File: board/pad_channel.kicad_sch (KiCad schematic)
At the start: 14 parts, among them J501 JST_B11P_XH_A, Q501 AO3400A, U501 SRV05-4

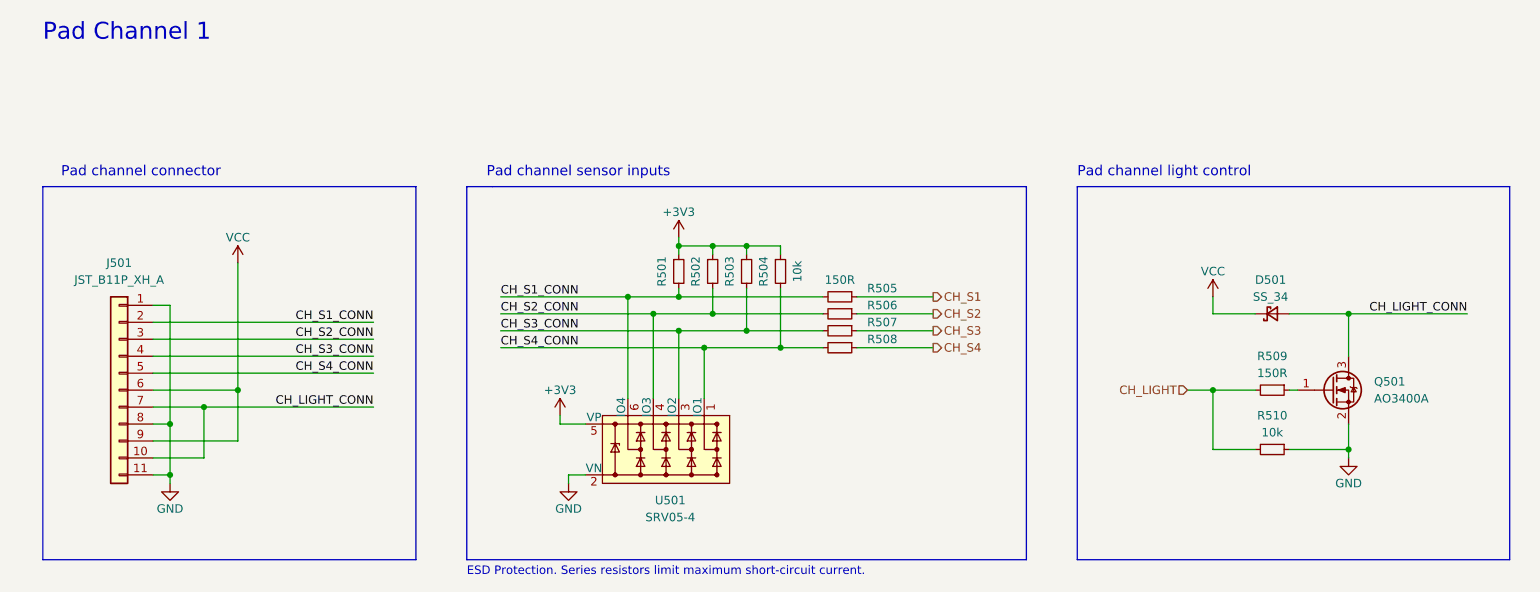
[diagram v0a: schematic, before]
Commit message: Schematic done
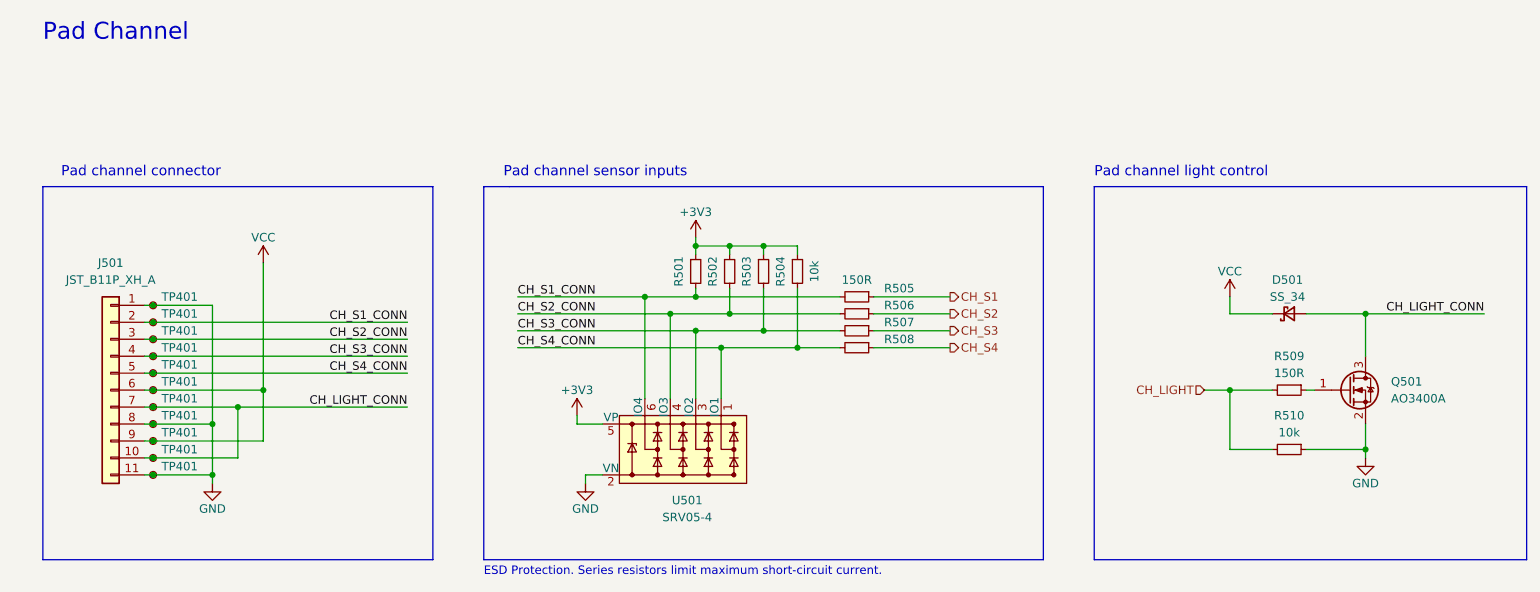
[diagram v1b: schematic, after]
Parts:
- added TP401 (x11): TestPoint_Small, TestPoint:TestPoint_Pad_D1.0mm, symbol Connector:TestPoint_Small
- D501: footprint (none) -> Diode_SMD:D_SMA
- J501: footprint (none) -> Connector_JST:JST_XH_B11B-XH-A_1x11_P2.50mm_Vertical
- R501, R502, R503, R504, R505, R506, R507, R508, R509, R510: footprint (none) -> Resistor_SMD:R_0603_1608Metric
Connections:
- net CH_LIGHT_CONN: now also TP401.1, TP401.1
- net CH_S1_CONN: now also TP401.1
- net CH_S2_CONN: now also TP401.1
- net CH_S3_CONN: now also TP401.1
- net CH_S4_CONN: now also TP401.1
- net GND: now also TP401.1, TP401.1, TP401.1
- net VCC: now also TP401.1, TP401.1
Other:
- note added: "Pad Channel"
- note removed: "Pad Channel 1"
- moved on the sheet: D501, J501, Q501, R501, R502, R503, R504, R505, R506, R507, R508, R509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

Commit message: Update PCB
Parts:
- removed TP401 (x11): TestPoint_Small, TestPoint:TestPoint_Pad_D1.0mm, symbol Connector:TestPoint_Small
- J501: footprint Connector_JST:JST_XH_B11B-XH-A_1x11_P2.50mm_Vertical -> ProjectLibrary:JST_NH_B11P-SHF-1AA_1x11_P2.50mm_Vertical
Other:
- moved on the sheet: J501

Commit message: Update PCB
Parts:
- J501: value JST_B11P_XH_A -> JST_B11P_SHF_1AA
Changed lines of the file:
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@@
       (effects (font (size 1.27 1.27)))
     )
-    (property "Value" "JST_B11P_XH_A" (at 45.72 87.63 0)
+    (property "Value" "JST_B11P_SHF_1AA" (at 45.72 87.63 0)
       (effects (font (size 1.27 1.27)))
     )
@@
       (project "bd845-pwb"
         (path "/c0443f53-6229-4858-b0f1-180b8ed8e6c2/ee25ad23-16ad-410b-9d51-44517f0b44fd"
-          (reference "J501") (unit 1) (value "JST_B11P_XH_A") (footprint "ProjectLibrary:JST_NH_B11P-SHF-1AA_1x11_P2.50mm_Vertical")
+          (reference "J501") (unit 1) (value "JST_B11P_SHF_1AA") (footprint "ProjectLibrary:JST_NH_B11P-SHF-1AA_1x11_P2.50mm_Vertical")
         )
         (path "/c0443f53-6229-4858-b0f1-180b8ed8e6c2"
-          (reference "J?") (unit 1) (value "JST_B11P_XH_A") (footprint "ProjectLibrary:JST_NH_B11P-SHF-1AA_1x11_P2.50mm_Vertical")
+          (reference "J?") (unit 1) (value "JST_B11P_SHF_1AA") (footprint "ProjectLibrary:JST_NH_B11P-SHF-1AA_1x11_P2.50mm_Vertical")
         )
         (path "/c0443f53-6229-4858-b0f1-180b8ed8e6c2/015ef0e1-80e9-4654-9c4e-55b9441615f7"
-          (reference "J601") (unit 1) (value "JST_B11P_XH_A") (footprint "ProjectLibrary:JST_NH_B11P-SHF-1AA_1x11_P2.50mm_Vertical")
+          (reference "J601") (unit 1) (value "JST_B11P_SHF_1AA") (footprint "ProjectLibrary:JST_NH_B11P-SHF-1AA_1x11_P2.50mm_Vertical")
         )
         (path "/c0443f53-6229-4858-b0f1-180b8ed8e6c2/37707cb0-7f1b-48ab-92b0-b85156a41fb4"
-          (reference "J701") (unit 1) (value "JST_B11P_XH_A") (footprint "ProjectLibrary:JST_NH_B11P-SHF-1AA_1x11_P2.50mm_Vertical")
+          (reference "J701") (unit 1) (value "JST_B11P_SHF_1AA") (footprint "ProjectLibrary:JST_NH_B11P-SHF-1AA_1x11_P2.50mm_Vertical")
         )
         (path "/c0443f53-6229-4858-b0f1-180b8ed8e6c2/b2b651a3-bec8-464c-9fa6-949dcdfcb350"
-          (reference "J801") (unit 1) (value "JST_B11P_XH_A") (footprint "ProjectLibrary:JST_NH_B11P-SHF-1AA_1x11_P2.50mm_Vertical")
+          (reference "J801") (unit 1) (value "JST_B11P_SHF_1AA") (footprint "ProjectLibrary:JST_NH_B11P-SHF-1AA_1x11_P2.50mm_Vertical")
         )
         (path "/c0443f53-6229-4858-b0f1-180b8ed8e6c2/79086545-f042-4543-848f-41bdcf514c29"

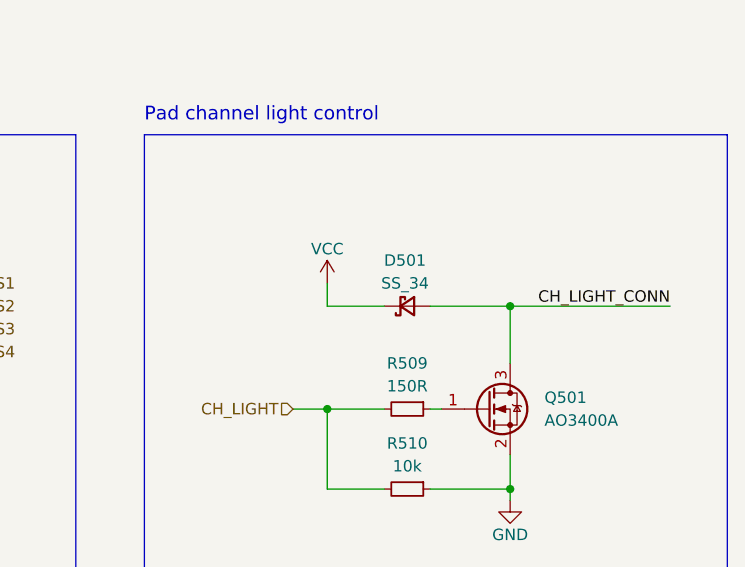
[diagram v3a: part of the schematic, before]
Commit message: Select input TVS diode
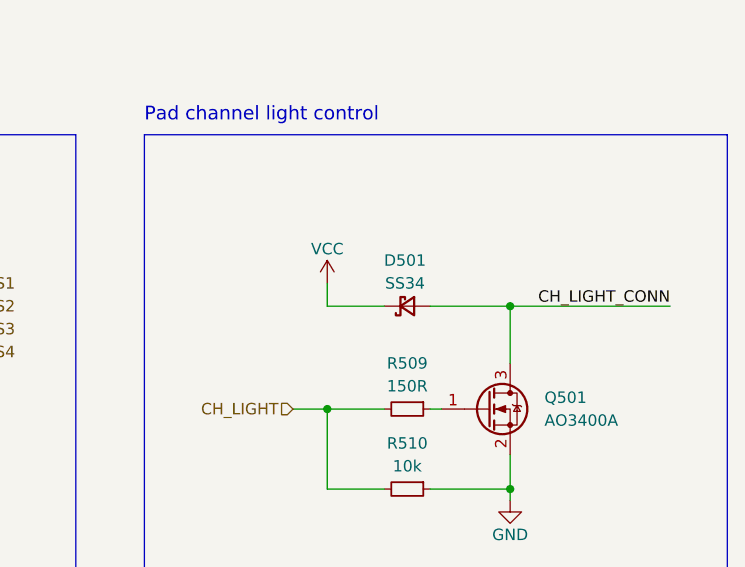
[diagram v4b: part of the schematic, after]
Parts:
- D501: value SS_34 -> SS34
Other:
- title: BD845-PWB -> BD845-PWB SCH
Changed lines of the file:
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@@
   (paper "A4")
   (title_block
-    (title "BD845-PWB")
+    (title "BD845-PWB SCH")
     (date "2022-11-27")
-    (rev "1")
+    (rev "1.0.0")
     (company "BlueDot, Vincenzo Fortunato")
   )
@@
       (effects (font (size 1.27 1.27)))
     )
-    (property "Value" "SS_34" (at 219.456 90.17 0)
+    (property "Value" "SS34" (at 219.456 90.17 0)
       (effects (font (size 1.27 1.27)))
     )
@@
       (project "bd845-pwb"
         (path "/c0443f53-6229-4858-b0f1-180b8ed8e6c2/ee25ad23-16ad-410b-9d51-44517f0b44fd"
-          (reference "D501") (unit 1) (value "SS_34") (footprint "Diode_SMD:D_SMA")
+          (reference "D501") (unit 1) (value "SS34") (footprint "Diode_SMD:D_SMA")
         )
         (path "/c0443f53-6229-4858-b0f1-180b8ed8e6c2"
@@
         )
         (path "/c0443f53-6229-4858-b0f1-180b8ed8e6c2/015ef0e1-80e9-4654-9c4e-55b9441615f7"
-          (reference "D601") (unit 1) (value "SS_34") (footprint "Diode_SMD:D_SMA")
-        )
-        (path "/c0443f53-6229-4858-b0f1-180b8ed8e6c2/37707cb0-7f1b-48ab-92b0-b85156a41fb4"
-          (reference "D701") (unit 1) (value "SS_34") (footprint "Diode_SMD:D_SMA")
-        )
-        (path "/c0443f53-6229-4858-b0f1-180b8ed8e6c2/b2b651a3-bec8-464c-9fa6-949dcdfcb350"
-          (reference "D801") (unit 1) (value "SS_34") (footprint "Diode_SMD:D_SMA")
-        )
-        (path "/c0443f53-6229-4858-b0f1-180b8ed8e6c2/79086545-f042-4543-848f-41bdcf514c29"
-          (reference "D901") (unit 1) (value "SS_34") (footprint "Diode_SMD:D_SMA")
-        )
-      )
+          (reference "D601") (unit 1) (value "SS34") (footprint "Diode_SMD:D_SMA")
+        )
+        (path "/c0443f53-6229-4858-b0f1-180b8ed8e6c2/37707cb0-7f1b-48ab-92b0-b85156a41fb4"
+          (reference "D701") (unit 1) (value "SS34") (footprint "Diode_SMD:D_SMA")
+        )
+        (path "/c0443f53-6229-4858-b0f1-180b8ed8e6c2/b2b651a3-bec8-464c-9fa6-949dcdfcb350"
+          (reference "D801") (unit 1) (value "SS34") (footprint "Diode_SMD:D_SMA")
+        )
+        (path "/c0443f53-6229-4858-b0f1-180b8ed8e6c2/79086545-f042-4543-848f-41bdcf514c29"
+          (reference "D901") (unit 1) (value "SS34") (footprint "Diode_SMD:D_SMA")
+        )
+      )
